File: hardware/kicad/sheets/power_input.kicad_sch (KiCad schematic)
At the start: 5 parts, among them J2 12V IN

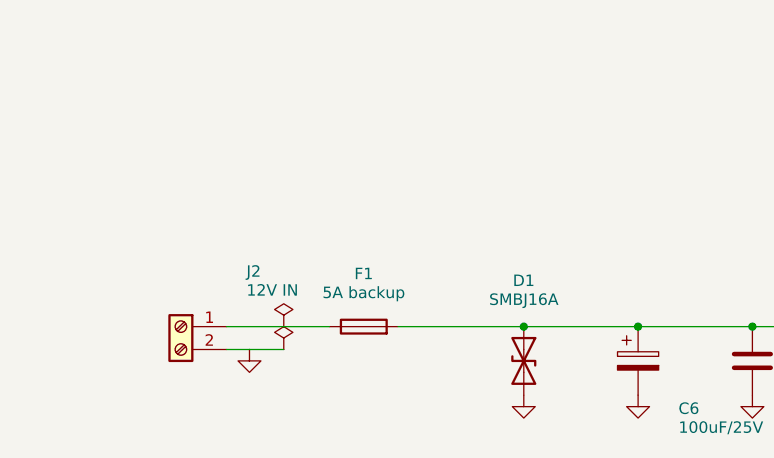
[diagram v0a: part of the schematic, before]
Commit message: Put supply pins on top and grounds on the bottom of IC symbols; flake8-clean Python
Schematic: re-laid out pins on U2, U3, U6, U7, U11, U14, U17-U20, U22-U24
and PS1 (supply on top, ground/strap pins on the bottom edge) via custom
`cryocooler:` symbols (make_lib.from_stock) and a gnd_bus helper; U18/U2
use mirroring instead of a 180 degree rotation. Nets are unchanged (ERC 0,
117/117 datasheet rules, PCB nets still match). Text placement now shows
every power-symbol name, avoids wires, and uses a realistic character width.

Python: black -l 79 -S plus manual wrapping so hardware/kicad and scripts/
pass flake8; add .flake8.

Co-Authored-By: Claude Sonnet 5.5 <noreply@anthropic.com>
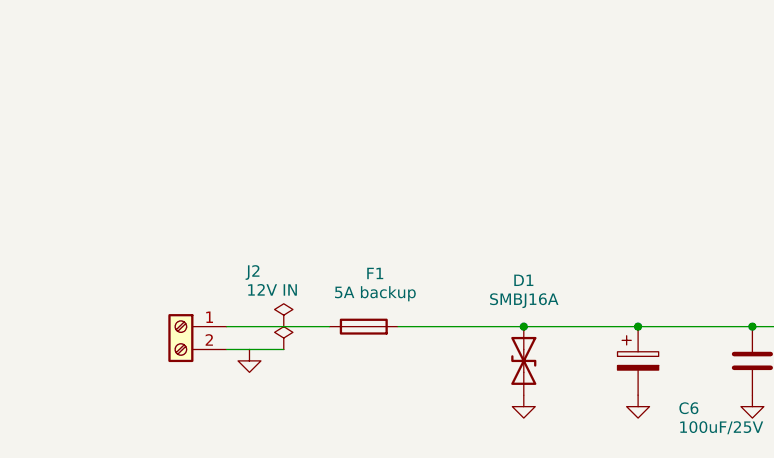
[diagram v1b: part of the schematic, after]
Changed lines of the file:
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@@
+	)
+	(junction
+		(at 76.2 76.2)
+		(diameter 0)
+		(color 0 0 0 0)
 	)
 	(junction
@@
 		(color 0 0 0 0)
 	)
-	(junction
-		(at 76.2 76.2)
-		(diameter 0)
-		(color 0 0 0 0)
-	)
 	(wire
 		(pts
@@
 	(wire
 		(pts
-			(xy 49.53 76.2) (xy 54.61 76.2)
+			(xy 88.9 76.2) (xy 101.6 76.2)
 		)
 		(stroke
@@
 	(wire
 		(pts
-			(xy 101.6 76.2) (xy 109.22 76.2)
+			(xy 43.18 76.2) (xy 49.53 76.2)
 		)
 		(stroke
@@
 	(wire
 		(pts
-			(xy 43.18 78.74) (xy 45.72 78.74)
+			(xy 76.2 76.2) (xy 88.9 76.2)
 		)
 		(stroke
@@
 	(wire
 		(pts
-			(xy 62.23 76.2) (xy 76.2 76.2)
+			(xy 43.18 78.74) (xy 45.72 78.74)
 		)
 		(stroke
@@
 	(wire
 		(pts
-			(xy 76.2 76.2) (xy 88.9 76.2)
+			(xy 62.23 76.2) (xy 76.2 76.2)
 		)
 		(stroke
@@
 	(wire
 		(pts
-			(xy 43.18 76.2) (xy 49.53 76.2)
+			(xy 101.6 76.2) (xy 109.22 76.2)
 		)
 		(stroke
@@
 	(wire
 		(pts
-			(xy 88.9 76.2) (xy 101.6 76.2)
+			(xy 49.53 76.2) (xy 54.61 76.2)
 		)
 		(stroke
@@
 		(dnp no)
 		(property "Reference" "F1"
-			(at 58.42 70.338 270)
+			(at 59.69 70.338 270)
 			(show_name no)
 			(do_not_autoplace no)
@@
 		)
 		(property "Value" "5A backup"
-			(at 58.42 72.438 270)
-			(show_name no)
-			(do_not_autoplace no)
+			(at 59.69 72.438 270)
+			(show_name no)
+			(do_not_autoplace no)

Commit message: KiCad schematic: INA239, ADS1220, SC18IS604 bridge, relay driver, test points
- system_current: INA237 -> INA239 (SPI, CS GPIO3) with the 49.9 ohm / 470 nF
  input filter, power LED and ALERT LED; VBUS shares the filtered IN- node.
- cold_head: ADS122C04 -> ADS1220 (SPI, CS GPIO44).
- i2c_bridge (new): SC18IS604 SPI-to-I2C bridge for the EMC2303, with a
  74LVC1G125 gating its MISO onto the shared bus.
- compressor_relay (new): GPIO16 high-side switch sharing one generator
  function with the amplifier REM switch.
- debug (new): about 40 test points and rail LEDs (the isolated rail LED
  returns to ISO_GND).
- ISO7741 -> ACS37800 SPI lines are straight wires (pins reordered on the
  symbol); USB_VBUS is one wire plus a naming label.
- Custom symbols for INA239, ADS1220, SC18IS604; datasheet rules 117 -> 162;
  GPIO map checks updated. ERC 0.

Co-Authored-By: Claude Sonnet 5.5 <noreply@anthropic.com>
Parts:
- removed C7: 100nF, Capacitor_SMD:C_0805_2012Metric, symbol Device:C
- added D1: SMBJ16A, Diode_SMD:D_SMB, symbol Device:D_TVS
- C7: renamed from D1; value SMBJ16A -> 100nF; footprint Diode_SMD:D_SMB -> Capacitor_SMD:C_0805_2012Metric; symbol Device:D_TVS -> Device:C
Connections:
- net GND: now also D1.2 (A2)
- net VIN: now also D1.1 (A1)

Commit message: Swap F1 to the Littelfuse NANO2 453 footprint and re-route
F1 is now the 5 A fast-acting Littelfuse 0453005.MR (2410 package); there is
no 5 A fast-acting fuse in 1812. Schematic, PCB (DRC 0 errors, 0 unconnected,
807/807 pad nets), Gerbers, BOM and notes regenerated.

Co-Authored-By: Claude Sonnet 5.5 <noreply@anthropic.com>
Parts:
- F1: footprint Fuse:Fuse_1812_4532Metric -> Fuse:Fuse_Littelfuse-NANO2-451_453
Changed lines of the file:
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@@
 			)
 		)
-		(property "Footprint" "Fuse:Fuse_1812_4532Metric"
+		(property "Footprint" "Fuse:Fuse_Littelfuse-NANO2-451_453"
 			(at 58.42 76.2 0)
 			(hide yes)
